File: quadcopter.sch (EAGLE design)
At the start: 81 parts, among them J1 ISP, J3 JUMPER, U2 ATMEGA128RFA1, Y1 16MHz

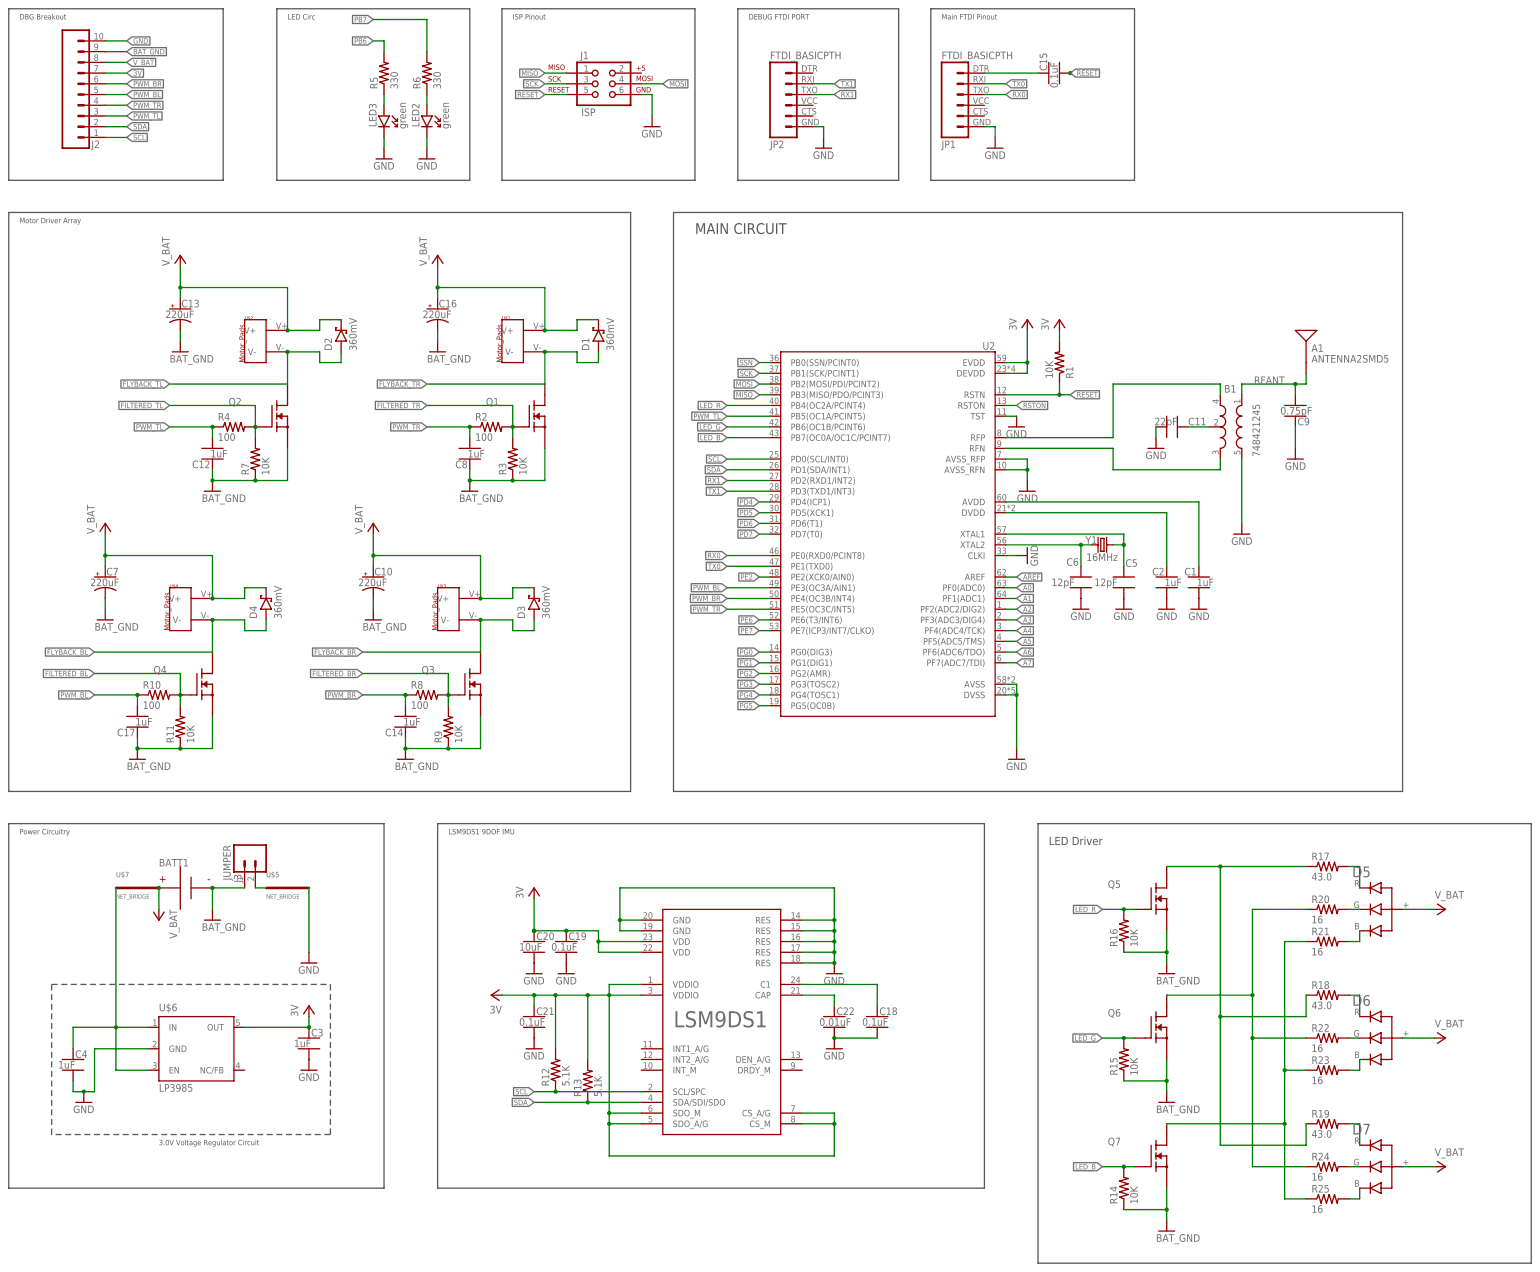
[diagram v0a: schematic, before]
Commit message: Fixed a few errors. Revised schematic and docs for new LEDs
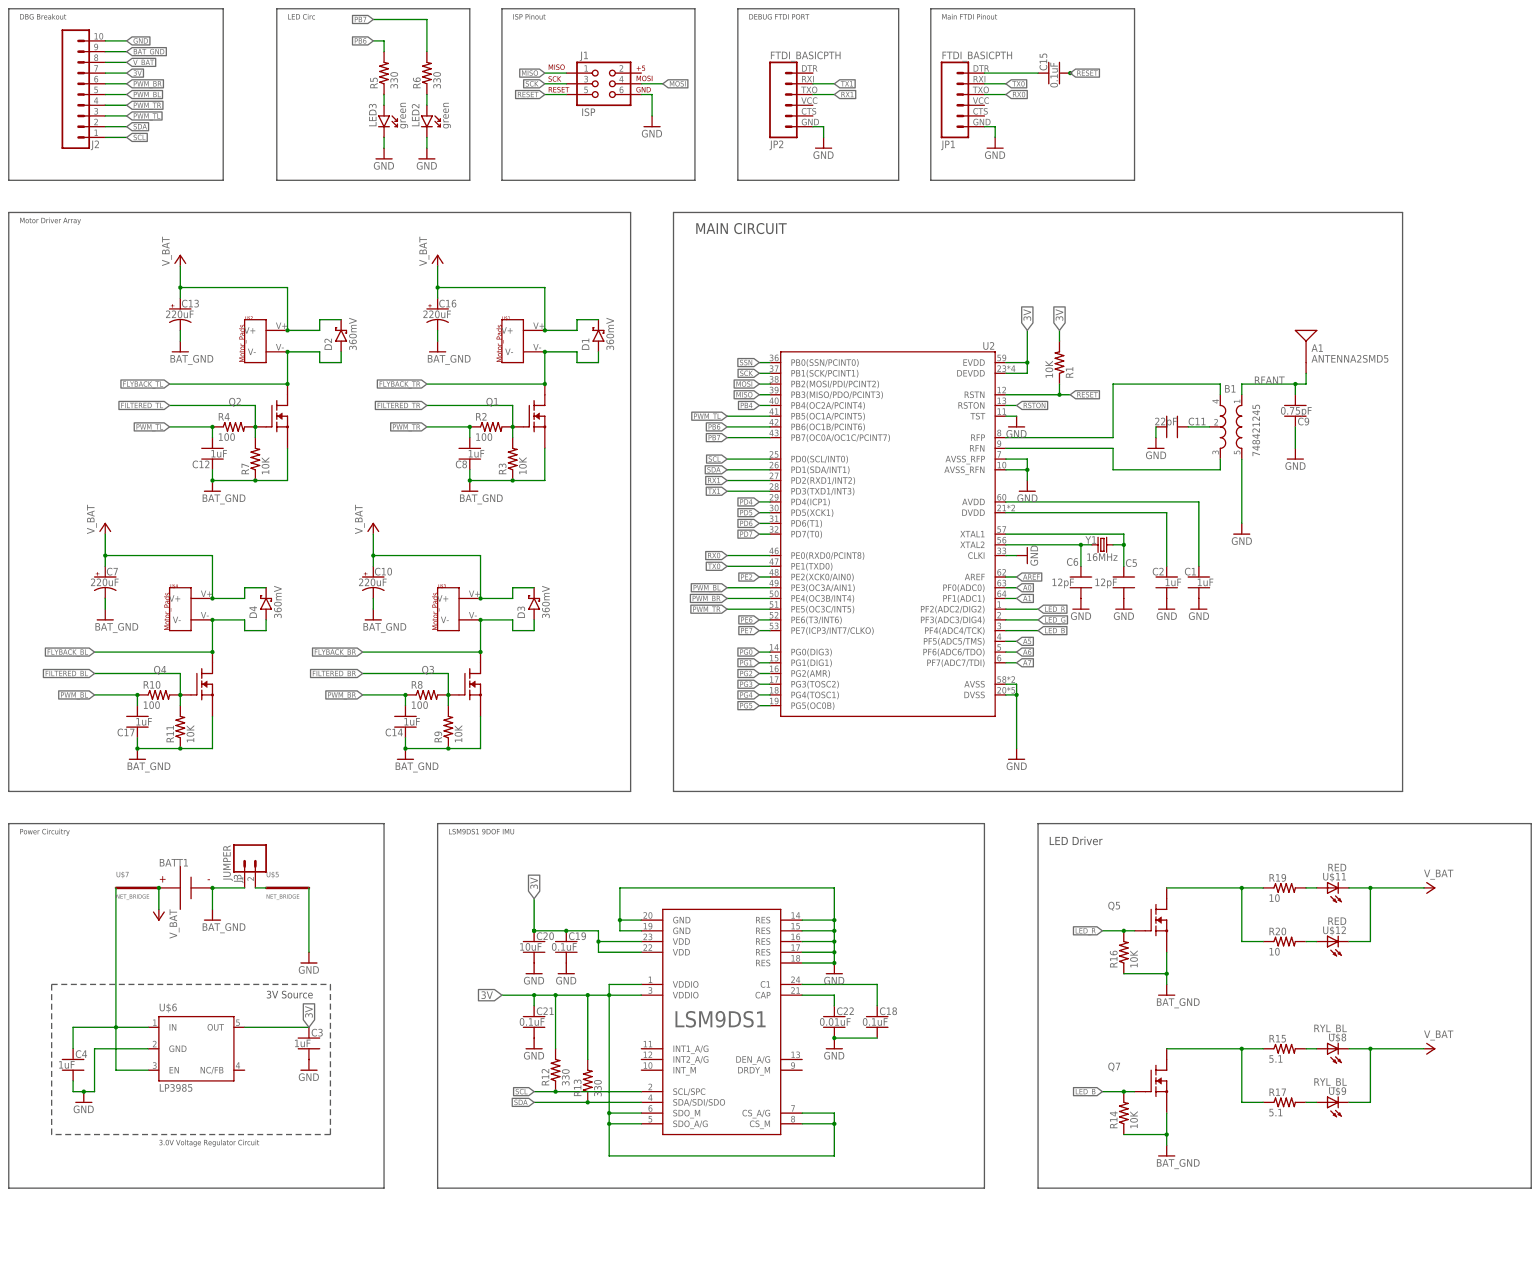
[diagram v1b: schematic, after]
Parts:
- removed D5, D6, D7: RGB_LED-C19HE1WT, quadparts:RGB_LED-C19HE1WT
- removed Q6: (no value), quadparts:NMOS-SI2302CDS
- removed R18: 43.0, quadparts_prebuilt:RESISTOR_SMD-2012-0805-43.0
- removed R21, R22, R23, R24, R25: 16, quadparts_prebuilt:RESISTOR_SMD-2012-0805-16
- added U$11, U$12: RED, LEDS:XQ-A-LED-RED-1616
- added U$8, U$9: RYL_BL, LEDS:XQ-A-LED-RYL-BL-1616
- R12, R13: value 5.1K -> 330; device quadparts_prebuilt:RESISTOR_SMD-2012-0805-5.1K -> quadparts_prebuilt:RESISTOR_SMD-2012-0805-330
- R15: value 10K -> 5.1; device quadparts_prebuilt:RESISTOR_SMD-2012-0805-10K -> quadparts:RESISTOR-ERJ-6D-5.1
- R17: value 43.0 -> 5.1; device quadparts_prebuilt:RESISTOR_SMD-2012-0805-43.0 -> quadparts:RESISTOR-ERJ-6D-5.1
- R19: value 43.0 -> 10; device quadparts_prebuilt:RESISTOR_SMD-2012-0805-43.0 -> quadparts:RESISTOR-ERJ-PO6-10
- R20: value 16 -> 10; device quadparts_prebuilt:RESISTOR_SMD-2012-0805-16 -> quadparts:RESISTOR-ERJ-PO6-10
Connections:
- removed net A2: U2.PF2(ADC2/DIG2)
- removed net A3: U2.PF3(ADC3/DIG4)
- removed net A4: U2.PF4(ADC4/TCK)
- removed net N$14: Q5.D, R17.1, R18.1, R19.1
- removed net N$17: D5.P$1, R17.2
- removed net N$18: D5.P$2, R20.2
- removed net N$19: Q6.D, R20.1, R22.1, R24.1
- removed net N$20: D6.P$1, R18.2
- removed net N$21: D7.P$1, R19.2
- new net PB4: U2.PB4(OC2A/PCINT4)
- net BAT_GND: no longer Q6.S, R15.1
- net LED_B: now also U2.PF4(ADC4/TCK); no longer U2.PB7(OC0A/OC1C/PCINT7)
- net LED_G: now also U2.PF3(ADC3/DIG4); no longer Q6.G, R15.2, U2.PB6(OC1B/PCINT6)
- net LED_R: now also U2.PF2(ADC2/DIG2); no longer U2.PB4(OC2A/PCINT4)
- net N$10: now also Q7.D, R15.1, R17.1; no longer D6.P$3, R23.2
- net N$11: now also R19.2, U$11.A; no longer D7.P$3, R25.2
- net N$12: now also R20.2, U$12.A; no longer Q7.D, R21.1, R23.1, R25.1
- net N$15: now also R15.2, U$8.A; no longer D7.P$2, R24.2
- net N$16: now also R17.2, U$9.A; no longer D6.P$2, R22.2
- net N$6: now also Q5.D, R19.1, R20.1; no longer D5.P$3, R21.2
- net PB6: now also U2.PB6(OC1B/PCINT6)
- net PB7: now also U2.PB7(OC0A/OC1C/PCINT7)
- net V_BAT: now also U$11.C, U$12.C, U$8.C, U$9.C; no longer D5.P$4, D6.P$4, D7.P$4
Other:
- note added: "3V Source"
- moved on the sheet: Q5, Q7, R14, R15, R16, R17, R19, R20

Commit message: Forgot to commit libraries. Fixed a few errors found on Eagle LINT.
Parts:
- renumbered U$11 to D5, U$12 to D6, U$8 to D7, U$9 to D8
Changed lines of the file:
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@@
 <part name="R14" library="quadparts_prebuilt" deviceset="RESISTOR_" device="SMD-2012-0805-10K" value="10K"/>
 <part name="R16" library="quadparts_prebuilt" deviceset="RESISTOR_" device="SMD-2012-0805-10K" value="10K"/>
-<part name="U$8" library="LEDS" deviceset="XQ-A-LED" device="-RYL-BL-1616" value="RYL_BL"/>
-<part name="U$9" library="LEDS" deviceset="XQ-A-LED" device="-RYL-BL-1616" value="RYL_BL"/>
-<part name="U$11" library="LEDS" deviceset="XQ-A-LED" device="-RED-1616" value="RED"/>
-<part name="U$12" library="LEDS" deviceset="XQ-A-LED" device="-RED-1616" value="RED"/>
 <part name="P+1" library="quadparts_prebuilt" deviceset="VCC" device="" value="V_BAT"/>
 <part name="P+2" library="quadparts_prebuilt" deviceset="VCC" device="" value="V_BAT"/>
@@
 <part name="R19" library="quadparts" deviceset="RESISTOR" device="-ERJ-PO6-10" value="10"/>
 <part name="R20" library="quadparts" deviceset="RESISTOR" device="-ERJ-PO6-10" value="10"/>
+<part name="D5" library="LEDS" deviceset="XQ-A-LED" device="-RED-1616" value="RED"/>
+<part name="D6" library="LEDS" deviceset="XQ-A-LED" device="-RED-1616" value="RED"/>
+<part name="D7" library="LEDS" deviceset="XQ-A-LED" device="-RYL-BL-1616" value="RYL_BL"/>
+<part name="D8" library="LEDS" deviceset="XQ-A-LED" device="-RYL-BL-1616" value="RYL_BL"/>
 </parts>
 <sheets>
@@
 <instance part="R14" gate="G$1" x="116.84" y="-109.22" rot="R90"/>
 <instance part="R16" gate="G$1" x="116.84" y="-71.12" rot="R90"/>
-<instance part="U$8" gate="G$1" x="165.1" y="-93.98" rot="R90"/>
-<instance part="U$9" gate="G$1" x="165.1" y="-106.68" rot="R90"/>
-<instance part="U$11" gate="G$1" x="165.1" y="-55.88" rot="R90"/>
-<instance part="U$12" gate="G$1" x="165.1" y="-68.58" rot="R90"/>
 <instance part="P+1" gate="VCC" x="190.5" y="-93.98" rot="R270"/>
 <instance part="P+2" gate="VCC" x="190.5" y="-55.88" rot="R270"/>
@@
 <instance part="R19" gate="G$1" x="154.94" y="-55.88"/>
 <instance part="R20" gate="G$1" x="154.94" y="-68.58"/>
+<instance part="D5" gate="G$1" x="165.1" y="-55.88" rot="R90"/>
+<instance part="D6" gate="G$1" x="165.1" y="-68.58" rot="R90"/>
+<instance part="D7" gate="G$1" x="165.1" y="-93.98" rot="R90"/>
+<instance part="D8" gate="G$1" x="165.1" y="-106.68" rot="R90"/>
 </instances>
 <busses>
@@
 </segment>
 <segment>
-<pinref part="U$12" gate="G$1" pin="C"/>
 <wire x1="175.26" y1="-68.58" x2="170.18" y2="-68.58" width="0.1524" layer="91"/>
-<pinref part="U$11" gate="G$1" pin="C"/>
 <wire x1="170.18" y1="-55.88" x2="175.26" y2="-55.88" width="0.1524" layer="91"/>
 <wire x1="175.26" y1="-55.88" x2="175.26" y2="-68.58" width="0.1524" layer="91"/>
@@
 <wire x1="175.26" y1="-55.88" x2="187.96" y2="-55.88" width="0.1524" layer="91"/>
 <junction x="175.26" y="-55.88"/>
-</segment>
-<segment>
-<pinref part="U$9" gate="G$1" pin="C"/>
+<pinref part="D5" gate="G$1" pin="C"/>
+<pinref part="D6" gate="G$1" pin="C"/>
+</segment>
+<segment>
 <wire x1="175.26" y1="-106.68" x2="170.18" y2="-106.68" width="0.1524" layer="91"/>
 <wire x1="175.26" y1="-106.68" x2="175.26" y2="-93.98" width="0.1524" layer="91"/>
-<pinref part="U$8" gate="G$1" pin="C"/>
 <wire x1="175.26" y1="-93.98" x2="170.18" y2="-93.98" width="0.1524" layer="91"/>
 <pinref part="P+1" gate="VCC" pin="VCC"/>
 <wire x1="175.26" y1="-93.98" x2="187.96" y2="-93.98" width="0.1524" layer="91"/>
 <junction x="175.26" y="-93.98"/>
+<pinref part="D7" gate="G$1" pin="C"/>
+<pinref part="D8" gate="G$1" pin="C"/>
 </segment>
 </net>
@@
 <net name="N$11" class="0">
 <segment>
-<pinref part="U$11" gate="G$1" pin="A"/>
 <wire x1="160.02" y1="-55.88" x2="162.56" y2="-55.88" width="0.1524" layer="91"/>
 <pinref part="R19" gate="G$1" pin="2"/>
+<pinref part="D5" gate="G$1" pin="A"/>
 </segment>
 </net>
 <net name="N$12" class="0">
 <segment>
-<pinref part="U$12" gate="G$1" pin="A"/>
 <wire x1="160.02" y1="-68.58" x2="162.56" y2="-68.58" width="0.1524" layer="91"/>
 <pinref part="R20" gate="G$1" pin="2"/>
+<pinref part="D6" gate="G$1" pin="A"/>
 </segment>
 </net>
 <net name="N$15" class="0">
 <segment>
-<pinref part="U$8" gate="G$1" pin="A"/>
 <wire x1="160.02" y1="-93.98" x2="162.56" y2="-93.98" width="0.1524" layer="91"/>
 <pinref part="R15" gate="G$1" pin="2"/>
+<pinref part="D7" gate="G$1" pin="A"/>
 </segment>
 </net>
 <net name="N$16" class="0">
 <segment>
-<pinref part="U$9" gate="G$1" pin="A"/>
 <wire x1="160.02" y1="-106.68" x2="162.56" y2="-106.68" width="0.1524" layer="91"/>
 <pinref part="R17" gate="G$1" pin="2"/>
-</segment>
-</net>
+<pinref part="D8" gate="G$1" pin="A"/>
+</segment>
+</net>

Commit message: Fixed jumper placement and PWM pin input.
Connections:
- net LED_G renamed A3
- removed net PB4: U2.PB4(OC2A/PCINT4)
- removed net PG5: U2.PG5(OC0B)
- new net A2: U2.PF2(ADC2/DIG2)
- new net A4: U2.PF4(ADC4/TCK)
- net BAT_GND: now also J3.2, U$5.P$1; no longer BATT1.N, J3.1
- net LED_B: now also U2.PG5(OC0B); no longer U2.PF4(ADC4/TCK)
- net LED_R: now also U2.PB4(OC2A/PCINT4); no longer U2.PF2(ADC2/DIG2)
- net N$2: now also BATT1.N, J3.1; no longer J3.2, U$5.P$1
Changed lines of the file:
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@@
 <instance part="U$7" gate="G$1" x="-116.84" y="-55.88"/>
 <instance part="C3" gate="G$1" x="-76.2" y="-91.44"/>
-<instance part="GND20" gate="1" x="-99.06" y="-63.5"/>
+<instance part="GND20" gate="1" x="-86.36" y="-63.5"/>
 <instance part="GND4" gate="1" x="-116.84" y="-25.4"/>
 <instance part="GND5" gate="1" x="-53.34" y="-25.4"/>
@@
 </segment>
 </net>
-<net name="PG5" class="0">
-<segment>
-<wire x1="33.02" y1="-12.7" x2="30.48" y2="-12.7" width="0.1524" layer="91"/>
-<label x="30.48" y="-12.7" size="1.27" layer="95" rot="MR0" xref="yes"/>
-<pinref part="U2" gate="G$1" pin="PG5(OC0B)"/>
-</segment>
-</net>
 <net name="PG2" class="0">
 <segment>
@@
 </segment>
 <segment>
-<pinref part="GND20" gate="1" pin="BAT_GND"/>
-<pinref part="BATT1" gate="G$1" pin="N"/>
-<wire x1="-99.06" y1="-60.96" x2="-99.06" y2="-55.88" width="0.1524" layer="91"/>
-<pinref part="J3" gate="G$1" pin="1"/>
-<wire x1="-99.06" y1="-55.88" x2="-91.44" y2="-55.88" width="0.1524" layer="91"/>
-<junction x="-99.06" y="-55.88"/>
-</segment>
-<segment>
 <pinref part="Q7" gate="G$1" pin="S"/>
 <pinref part="GND28" gate="1" pin="BAT_GND"/>
@@
 <wire x1="116.84" y1="-76.2" x2="127" y2="-76.2" width="0.1524" layer="91"/>
 <junction x="127" y="-76.2"/>
+</segment>
+<segment>
+<pinref part="J3" gate="G$1" pin="2"/>
+<pinref part="U$5" gate="G$1" pin="P$1"/>
+<wire x1="-88.9" y1="-55.88" x2="-86.36" y2="-55.88" width="0.1524" layer="91"/>
+<pinref part="GND20" gate="1" pin="BAT_GND"/>
+<wire x1="-86.36" y1="-60.96" x2="-86.36" y2="-55.88" width="0.1524" layer="91"/>
+<junction x="-86.36" y="-55.88"/>
 </segment>
 </net>
@@
 </segment>
 </net>
-<net name="N$2" class="0">
-<segment>
-<pinref part="J3" gate="G$1" pin="2"/>
-<pinref part="U$5" gate="G$1" pin="P$1"/>
-<wire x1="-88.9" y1="-55.88" x2="-86.36" y2="-55.88" width="0.1524" layer="91"/>
-</segment>
-</net>
 <net name="LED_R" class="0">
 <segment>
@@
 </segment>
 <segment>
-<wire x1="88.9" y1="10.16" x2="96.52" y2="10.16" width="0.1524" layer="91"/>
-<label x="96.52" y="10.16" size="1.27" layer="95" rot="MR180" xref="yes"/>
-<pinref part="U2" gate="G$1" pin="PF2(ADC2/DIG2)"/>
-</segment>
-</net>
-<net name="LED_G" class="0">
-<segment>
-<wire x1="88.9" y1="7.62" x2="96.52" y2="7.62" width="0.1524" layer="91"/>
-<label x="96.52" y="7.62" size="1.27" layer="95" rot="MR180" xref="yes"/>
+<wire x1="33.02" y1="58.42" x2="22.86" y2="58.42" width="0.1524" layer="91"/>
+<label x="22.86" y="58.42" size="1.27" layer="95" rot="MR0" xref="yes"/>
+<pinref part="U2" gate="G$1" pin="PB4(OC2A/PCINT4)"/>
+</segment>
+</net>
+<net name="A3" class="0">
+<segment>
+<wire x1="88.9" y1="7.62" x2="91.44" y2="7.62" width="0.1524" layer="91"/>
+<label x="91.44" y="7.62" size="1.27" layer="95" rot="MR180" xref="yes"/>
 <pinref part="U2" gate="G$1" pin="PF3(ADC3/DIG4)"/>
 </segment>
@@
 </segment>
 <segment>
-<wire x1="88.9" y1="5.08" x2="96.52" y2="5.08" width="0.1524" layer="91"/>
-<label x="96.52" y="5.08" size="1.27" layer="95" rot="MR180" xref="yes"/>
-<pinref part="U2" gate="G$1" pin="PF4(ADC4/TCK)"/>
-</segment>
-</net>
-<net name="PB4" class="0">
-<segment>
-<wire x1="33.02" y1="58.42" x2="30.48" y2="58.42" width="0.1524" layer="91"/>
-<label x="30.48" y="58.42" size="1.27" layer="95" rot="MR0" xref="yes"/>
-<pinref part="U2" gate="G$1" pin="PB4(OC2A/PCINT4)"/>
+<wire x1="33.02" y1="-12.7" x2="22.86" y2="-12.7" width="0.1524" layer="91"/>
+<label x="22.86" y="-12.7" size="1.27" layer="95" rot="MR0" xref="yes"/>
+<pinref part="U2" gate="G$1" pin="PG5(OC0B)"/>
 </segment>
 </net>
@@
 </segment>
 </net>
+<net name="A2" class="0">
+<segment>
+<wire x1="88.9" y1="10.16" x2="91.44" y2="10.16" width="0.1524" layer="91"/>
+<label x="91.44" y="10.16" size="1.27" layer="95" rot="MR180" xref="yes"/>
+<pinref part="U2" gate="G$1" pin="PF2(ADC2/DIG2)"/>
+</segment>
+</net>
+<net name="A4" class="0">
+<segment>
+<wire x1="88.9" y1="5.08" x2="91.44" y2="5.08" width="0.1524" layer="91"/>
+<label x="91.44" y="5.08" size="1.27" layer="95" rot="MR180" xref="yes"/>
+<pinref part="U2" gate="G$1" pin="PF4(ADC4/TCK)"/>
+</segment>
+</net>
+<net name="N$2" class="0">
+<segment>
+<pinref part="J3" gate="G$1" pin="1"/>
+<pinref part="BATT1" gate="G$1" pin="N"/>
+<wire x1="-91.44" y1="-55.88" x2="-99.06" y2="-55.88" width="0.1524" layer="91"/>
+</segment>
+</net>

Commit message: Commit design reviews and performed revisions requested.
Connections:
- net BAT_GND: now also BATT1.N; no longer J3.2
- net N$2: now also BATT1.P, J3.2; no longer BATT1.N, J3.1
- net V_BAT: now also J3.1; no longer BATT1.P
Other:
- moved on the sheet: BATT1, J3
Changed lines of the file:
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@@
 <instance part="P+8" gate="VCC" x="-124.46" y="30.48"/>
 <instance part="LSM9DS1" gate="G$1" x="20.32" y="-86.36"/>
-<instance part="BATT1" gate="G$1" x="-104.14" y="-55.88"/>
+<instance part="BATT1" gate="G$1" x="-93.98" y="-55.88"/>
 <instance part="J2" gate="G$1" x="-134.62" y="119.38"/>
 <instance part="U$5" gate="G$1" x="-81.28" y="-55.88"/>
@@
 <instance part="C22" gate="G$1" x="48.26" y="-86.36"/>
 <instance part="GND34" gate="1" x="48.26" y="-93.98"/>
-<instance part="J3" gate="G$1" x="-93.98" y="-45.72" rot="R270"/>
+<instance part="J3" gate="G$1" x="-111.76" y="-45.72" rot="R270"/>
 <instance part="R12" gate="G$1" x="-17.78" y="-99.06" rot="R90"/>
 <instance part="R13" gate="G$1" x="-10.16" y="-101.6" rot="R90"/>
@@
 </segment>
 <segment>
-<pinref part="BATT1" gate="G$1" pin="P"/>
-<wire x1="-111.76" y1="-55.88" x2="-111.76" y2="-60.96" width="0.1524" layer="91"/>
-<pinref part="P+9" gate="VCC" pin="VCC"/>
-<pinref part="U$7" gate="G$1" pin="P$2"/>
-<junction x="-111.76" y="-55.88"/>
-</segment>
-<segment>
 <wire x1="175.26" y1="-68.58" x2="170.18" y2="-68.58" width="0.1524" layer="91"/>
 <wire x1="170.18" y1="-55.88" x2="175.26" y2="-55.88" width="0.1524" layer="91"/>
@@
 <pinref part="D7" gate="G$1" pin="C"/>
 <pinref part="D8" gate="G$1" pin="C"/>
+</segment>
+<segment>
+<pinref part="U$7" gate="G$1" pin="P$2"/>
+<pinref part="P+9" gate="VCC" pin="VCC"/>
+<wire x1="-111.76" y1="-60.96" x2="-111.76" y2="-55.88" width="0.1524" layer="91"/>
+<pinref part="J3" gate="G$1" pin="1"/>
+<wire x1="-109.22" y1="-55.88" x2="-111.76" y2="-55.88" width="0.1524" layer="91"/>
+<junction x="-111.76" y="-55.88"/>
 </segment>
 </net>
@@
 </segment>
 <segment>
-<pinref part="J3" gate="G$1" pin="2"/>
 <pinref part="U$5" gate="G$1" pin="P$1"/>
-<wire x1="-88.9" y1="-55.88" x2="-86.36" y2="-55.88" width="0.1524" layer="91"/>
 <pinref part="GND20" gate="1" pin="BAT_GND"/>
 <wire x1="-86.36" y1="-60.96" x2="-86.36" y2="-55.88" width="0.1524" layer="91"/>
+<pinref part="BATT1" gate="G$1" pin="N"/>
+<wire x1="-88.9" y1="-55.88" x2="-86.36" y2="-55.88" width="0.1524" layer="91"/>
 <junction x="-86.36" y="-55.88"/>
 </segment>
@@
 <net name="N$2" class="0">
 <segment>
-<pinref part="J3" gate="G$1" pin="1"/>
-<pinref part="BATT1" gate="G$1" pin="N"/>
-<wire x1="-91.44" y1="-55.88" x2="-99.06" y2="-55.88" width="0.1524" layer="91"/>
-</segment>
-</net>
+<pinref part="J3" gate="G$1" pin="2"/>
+<pinref part="BATT1" gate="G$1" pin="P"/>
+<wire x1="-106.68" y1="-55.88" x2="-101.6" y2="-55.88" width="0.1524" layer="91"/>
+</segment>
+</net>
